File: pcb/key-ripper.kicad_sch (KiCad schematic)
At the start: 202 parts, among them SW1 ESC, SW2 TILDE, SW3 TAB, SW4 CAPS, SW5 L_SHIFT, SW6 FN

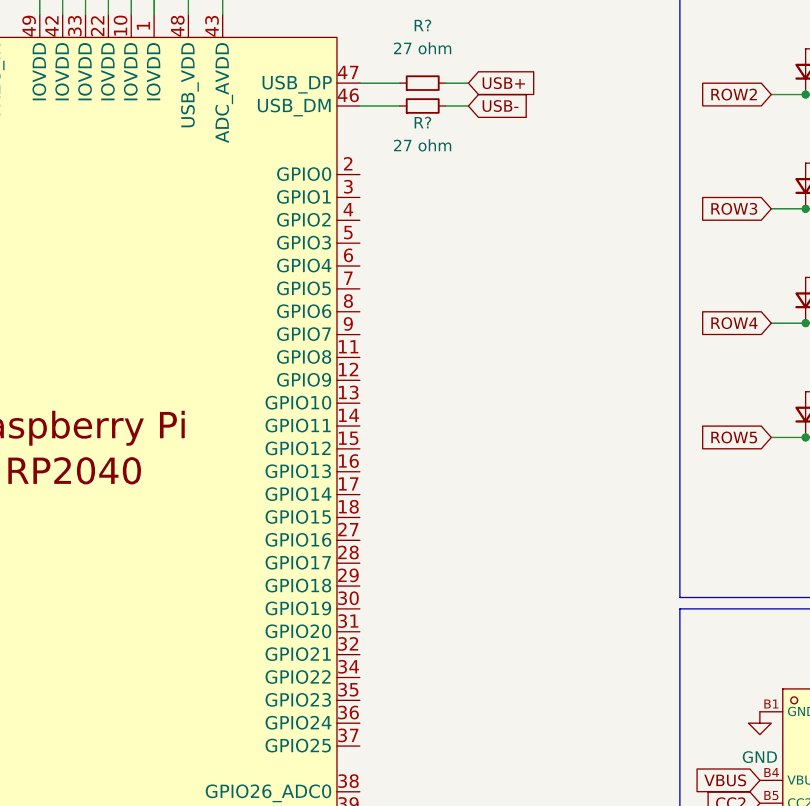
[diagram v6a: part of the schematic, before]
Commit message: Assign row/column connections to GPIO pins
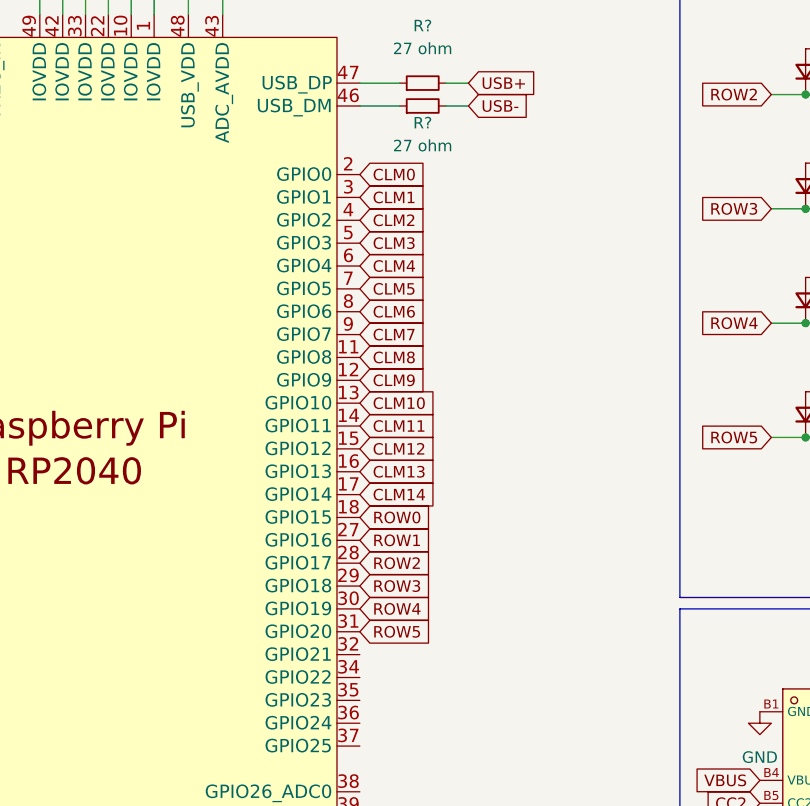
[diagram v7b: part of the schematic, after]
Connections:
- net CLM0: now also U?.2 (GPIO0)
- net CLM1: now also U?.3 (GPIO1)
- net CLM10: now also U?.13 (GPIO10)
- net CLM11: now also U?.14 (GPIO11)
- net CLM12: now also U?.15 (GPIO12)
- net CLM13: now also U?.16 (GPIO13)
- net CLM14: now also U?.17 (GPIO14)
- net CLM2: now also U?.4 (GPIO2)
- net CLM3: now also U?.5 (GPIO3)
- net CLM4: now also U?.6 (GPIO4)
- net CLM5: now also U?.7 (GPIO5)
- net CLM6: now also U?.8 (GPIO6)
- net CLM7: now also U?.9 (GPIO7)
- net CLM8: now also U?.11 (GPIO8)
- net CLM9: now also U?.12 (GPIO9)
- net ROW0: now also U?.18 (GPIO15)
- net ROW1: now also U?.27 (GPIO16)
- net ROW2: now also U?.28 (GPIO17)
- net ROW3: now also U?.29 (GPIO18)
- net ROW4: now also U?.30 (GPIO19)
- net ROW5: now also U?.31 (GPIO20)
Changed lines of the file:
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@@
+    )
+  )
+  (global_label "CLM4" (shape input) (at -22.86 73.66 0) (fields_autoplaced)
+    (effects (font (size 1.27 1.27)) (justify left))
+    (property "Intersheet References" "${INTERSHEET_REFS}" (id 0) (at -15.4879 73.7394 0)
+      (effects (font (size 1.27 1.27)) (justify left) hide)
     )
   )
@@
     )
   )
+  (global_label "CLM2" (shape input) (at -22.86 68.58 0) (fields_autoplaced)
+    (effects (font (size 1.27 1.27)) (justify left))
+    (property "Intersheet References" "${INTERSHEET_REFS}" (id 0) (at -15.4879 68.6594 0)
+      (effects (font (size 1.27 1.27)) (justify left) hide)
+    )
+  )
   (global_label "CLM3" (shape input) (at 82.55 96.52 270) (fields_autoplaced)
     (effects (font (size 1.27 1.27)) (justify right))
@@
     )
   )
+  (global_label "ROW5" (shape input) (at -22.86 114.3 0) (fields_autoplaced)
+    (effects (font (size 1.27 1.27)) (justify left))
+    (property "Intersheet References" "${INTERSHEET_REFS}" (id 0) (at -15.1855 114.3794 0)
+      (effects (font (size 1.27 1.27)) (justify left) hide)
+    )
+  )
   (global_label "CLM14" (shape input) (at 250.19 96.52 270) (fields_autoplaced)
     (effects (font (size 1.27 1.27)) (justify right))
@@
     )
   )
+  (global_label "CLM0" (shape input) (at -22.86 63.5 0) (fields_autoplaced)
+    (effects (font (size 1.27 1.27)) (justify left))
+    (property "Intersheet References" "${INTERSHEET_REFS}" (id 0) (at -15.4879 63.5794 0)
+      (effects (font (size 1.27 1.27)) (justify left) hide)
+    )
+  )
   (global_label "OSC_OUT" (shape input) (at 142.24 117.475 0) (fields_autoplaced)
     (effects (font (size 1.27 1.27)) (justify left))
@@
     )
   )
+  (global_label "CLM7" (shape input) (at -22.86 81.28 0) (fields_autoplaced)
+    (effects (font (size 1.27 1.27)) (justify left))
+    (property "Intersheet References" "${INTERSHEET_REFS}" (id 0) (at -15.4879 81.3594 0)
+      (effects (font (size 1.27 1.27)) (justify left) hide)
+    )
+  )
+  (global_label "CLM11" (shape input) (at -22.86 91.44 0) (fields_autoplaced)
+    (effects (font (size 1.27 1.27)) (justify left))
+    (property "Intersheet References" "${INTERSHEET_REFS}" (id 0) (at -14.2783 91.5194 0)
+      (effects (font (size 1.27 1.27)) (justify left) hide)
+    )
+  )
   (global_label "ROW1" (shape input) (at 22.86 41.91 180) (fields_autoplaced)
     (effects (font (size 1.27 1.27)) (justify right))
@@
     )
   )
+  (global_label "ROW3" (shape input) (at -22.86 109.22 0) (fields_autoplaced)
+    (effects (font (size 1.27 1.27)) (justify left))
+    (property "Intersheet References" "${INTERSHEET_REFS}" (id 0) (at -15.1855 109.2994 0)
+      (effects (font (size 1.27 1.27)) (justify left) hide)
+    )
+  )
   (global_label "USB+" (shape input) (at 44.45 138.43 0) (fields_autoplaced)
     (effects (font (size 1.27 1.27)) (justify left))
@@
     )
   )
+  (global_label "CLM8" (shape input) (at -22.86 83.82 0) (fields_autoplaced)
+    (effects (font (size 1.27 1.27)) (justify left))
+    (property "Intersheet References" "${INTERSHEET_REFS}" (id 0) (at -15.4879 83.8994 0)
+      (effects (font (size 1.27 1.27)) (justify left) hide)
+    )
+  )
   (global_label "CLM4" (shape input) (at 97.79 96.52 270) (fields_autoplaced)
     (effects (font (size 1.27 1.27)) (justify right))
@@
     )
   )
+  (global_label "CLM10" (shape input) (at -22.86 88.9 0) (fields_autoplaced)
+    (effects (font (size 1.27 1.27)) (justify left))
+    (property "Intersheet References" "${INTERSHEET_REFS}" (id 0) (at -14.2783 88.9794 0)
+      (effects (font (size 1.27 1.27)) (justify left) hide)
+    )
+  )
   (global_label "VBUS" (shape input) (at 21.59 130.81 180) (fields_autoplaced)
     (effects (font (size 1.27 1.27)) (justify right))
@@
     )
   )
+  (global_label "ROW0" (shape input) (at -22.86 101.6 0) (fields_autoplaced)
+    (effects (font (size 1.27 1.27)) (justify left))
+    (property "Intersheet References" "${INTERSHEET_REFS}" (id 0) (at -15.1855 101.6794 0)
+      (effects (font (size 1.27 1.27)) (justify left) hide)
+    )
+  )
+  (global_label "CLM3" (shape input) (at -22.86 71.12 0) (fields_autoplaced)
+    (effects (font (size 1.27 1.27)) (justify left))
+    (property "Intersheet References" "${INTERSHEET_REFS}" (id 0) (at -15.4879 71.1994 0)
+      (effects (font (size 1.27 1.27)) (justify left) hide)
+    )
+  )
   (global_label "ROW0" (shape input) (at 22.86 29.21 180) (fields_autoplaced)
     (effects (font (size 1.27 1.27)) (justify right))
@@
     )
   )
+  (global_label "CLM9" (shape input) (at -22.86 86.36 0) (fields_autoplaced)
+    (effects (font (size 1.27 1.27)) (justify left))
+    (property "Intersheet References" "${INTERSHEET_REFS}" (id 0) (at -15.4879 86.4394 0)
+      (effects (font (size 1.27 1.27)) (justify left) hide)
+    )
+  )
   (global_label "CC1" (shape input) (at 44.45 140.97 0) (fields_autoplaced)
     (effects (font (size 1.27 1.27)) (justify left))
@@
     )
   )
+  (global_label "CLM12" (shape input) (at -22.86 93.98 0) (fields_autoplaced)
+    (effects (font (size 1.27 1.27)) (justify left))
+    (property "Intersheet References" "${INTERSHEET_REFS}" (id 0) (at -14.2783 94.0594 0)
+      (effects (font (size 1.27 1.27)) (justify left) hide)
+    )
+  )
   (global_label "QSPI_SS" (shape input) (at -86.36 64.77 180) (fields_autoplaced)
     (effects (font (size 1.27 1.27)) (justify right))
@@
     )
   )
+  (global_label "CLM14" (shape input) (at -22.86 99.06 0) (fields_autoplaced)
+    (effects (font (size 1.27 1.27)) (justify left))
+    (property "Intersheet References" "${INTERSHEET_REFS}" (id 0) (at -14.2783 99.1394 0)
+      (effects (font (size 1.27 1.27)) (justify left) hide)
+    )
+  )
   (global_label "USB-" (shape input) (at -10.795 55.88 0) (fields_autoplaced)
     (effects (font (size 1.27 1.27)) (justify left))
@@
     )
   )
+  (global_label "ROW4" (shape input) (at -22.86 111.76 0) (fields_autoplaced)
+    (effects (font (size 1.27 1.27)) (justify left))
+    (property "Intersheet References" "${INTERSHEET_REFS}" (id 0) (at -15.1855 111.8394 0)
+      (effects (font (size 1.27 1.27)) (justify left) hide)
+    )
+  )
+  (global_label "CLM6" (shape input) (at -22.86 78.74 0) (fields_autoplaced)
+    (effects (font (size 1.27 1.27)) (justify left))
+    (property "Intersheet References" "${INTERSHEET_REFS}" (id 0) (at -15.4879 78.8194 0)
+      (effects (font (size 1.27 1.27)) (justify left) hide)
+    )
+  )
+  (global_label "ROW2" (shape input) (at -22.86 106.68 0) (fields_autoplaced)
+    (effects (font (size 1.27 1.27)) (justify left))
+    (property "Intersheet References" "${INTERSHEET_REFS}" (id 0) (at -15.1855 106.7594 0)
+      (effects (font (size 1.27 1.27)) (justify left) hide)
+    )
+  )
+  (global_label "ROW1" (shape input) (at -22.86 104.14 0) (fields_autoplaced)
+    (effects (font (size 1.27 1.27)) (justify left))
+    (property "Intersheet References" "${INTERSHEET_REFS}" (id 0) (at -15.1855 104.2194 0)
+      (effects (font (size 1.27 1.27)) (justify left) hide)
+    )
+  )
   (global_label "VBUS" (shape input) (at 44.45 143.51 0) (fields_autoplaced)
     (effects (font (size 1.27 1.27)) (justify left))
@@
     )
   )
+  (global_label "CLM13" (shape input) (at -22.86 96.52 0) (fields_autoplaced)
+    (effects (font (size 1.27 1.27)) (justify left))
+    (property "Intersheet References" "${INTERSHEET_REFS}" (id 0) (at -14.2783 96.5994 0)
+      (effects (font (size 1.27 1.27)) (justify left) hide)
+    )
+  )
   (global_label "CLM8" (shape input) (at 158.75 96.52 270) (fields_autoplaced)
     (effects (font (size 1.27 1.27)) (justify right))
@@
     )
   )
+  (global_label "CLM1" (shape input) (at -22.86 66.04 0) (fields_autoplaced)
+    (effects (font (size 1.27 1.27)) (justify left))
+    (property "Intersheet References" "${INTERSHEET_REFS}" (id 0) (at -15.4879 66.1194 0)
+      (effects (font (size 1.27 1.27)) (justify left) hide)
+    )
+  )
   (global_label "CLM13" (shape input) (at 234.95 96.52 270) (fields_autoplaced)
     (effects (font (size 1.27 1.27)) (justify right))
@@
     )
   )
+  (global_label "CLM5" (shape input) (at -22.86 76.2 0) (fields_autoplaced)
+    (effects (font (size 1.27 1.27)) (justify left))
+    (property "Intersheet References" "${INTERSHEET_REFS}" (id 0) (at -15.4879 76.2794 0)
+      (effects (font (size 1.27 1.27)) (justify left) hide)
+    )
+  )

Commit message: Typo fix
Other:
- note added: "Serial Wire Debug"
- note removed: "Seerial Wire Debug"
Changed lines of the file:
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@@
     (effects (font (size 1.27 1.27)) (justify left bottom))
   )
-  (text "Seerial Wire Debug" (at 171.45 139.065 0)
+  (text "Serial Wire Debug" (at 171.45 139.065 0)
     (effects (font (size 1.27 1.27)) (justify left bottom))
   )
